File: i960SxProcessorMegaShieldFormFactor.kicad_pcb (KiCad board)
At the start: 4 copper layers, 101.6 x 53.3 mm, 31 parts, among them P1 Power, P2 Data Lines Lower, P3 Data Lines Upper, P4 Address Lines, P5 PWM, P6 Serializable Pins, P7 1284p Direct Connection, U1 74HC245, U2 74HC245, U3 80960Sx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

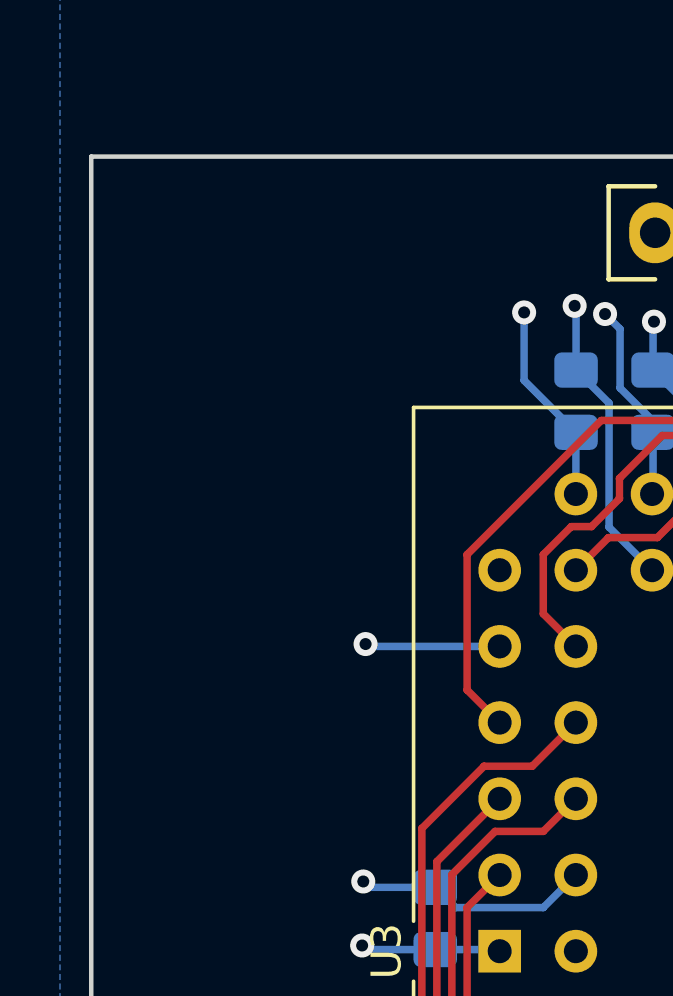
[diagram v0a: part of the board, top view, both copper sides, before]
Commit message: Added CC-BY-SA silk screen
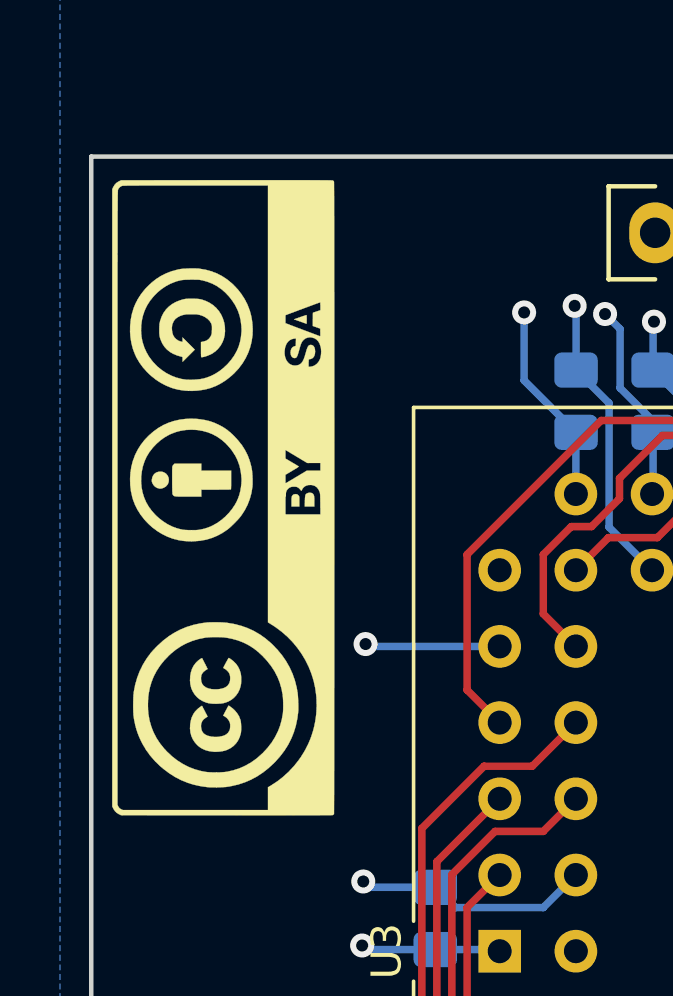
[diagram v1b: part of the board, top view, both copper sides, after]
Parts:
- added G***: LOGO, labitat/labitat_kicad_footprints.pretty:cc-by-sa_badge_8mm, F.Cu at (107.8, 79.7)

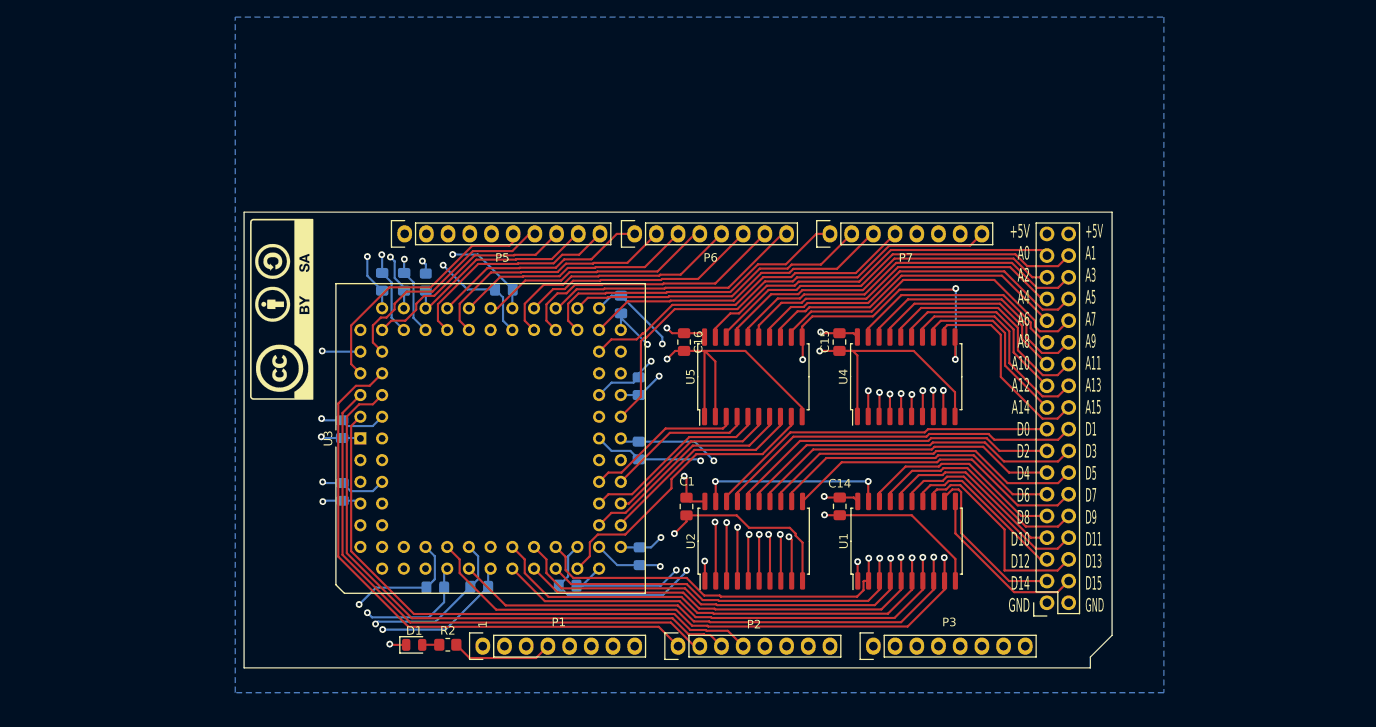
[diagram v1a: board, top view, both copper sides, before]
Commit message: Start placing different ics
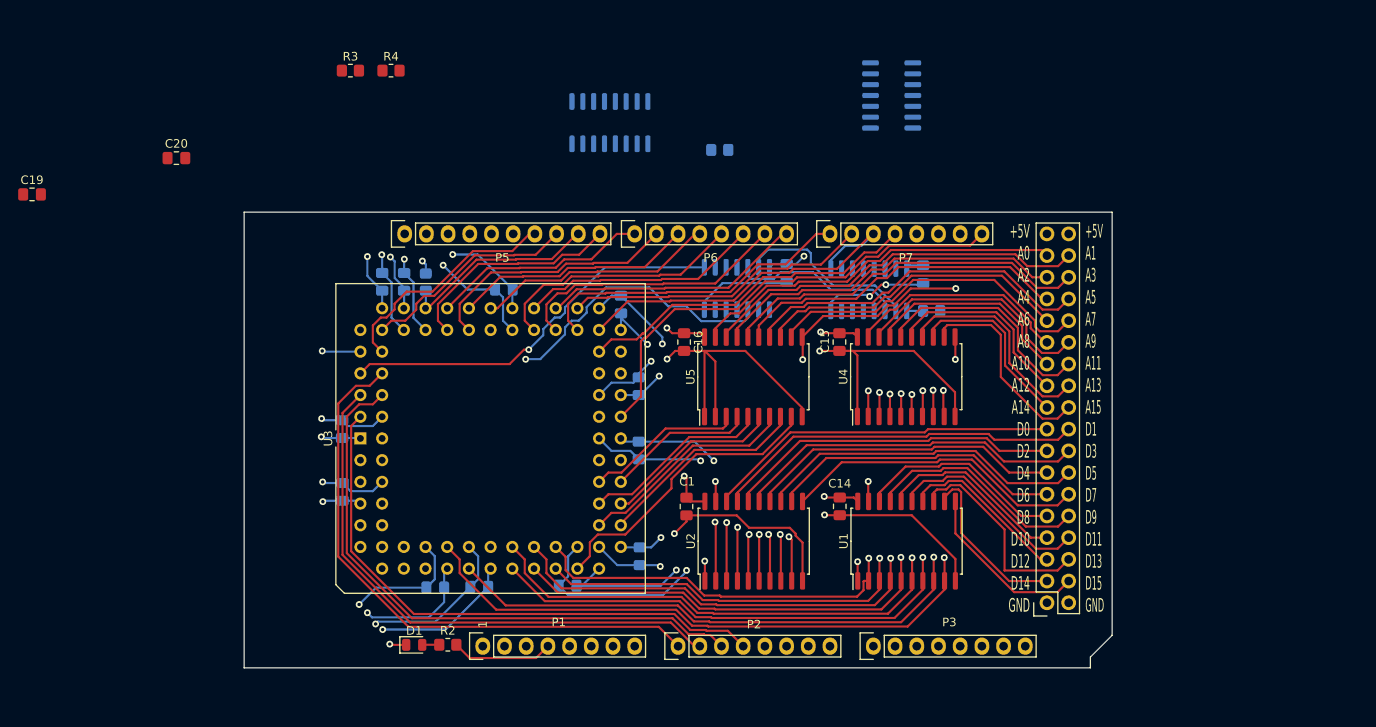
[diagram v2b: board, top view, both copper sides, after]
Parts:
- removed G***: LOGO, labitat/labitat_kicad_footprints.pretty:cc-by-sa_badge_8mm
- added C17: 0.1uF, Capacitor_SMD:C_0805_2012Metric_Pad1.18x1.45mm_HandSolder, B.Cu at (166.9, 75.4)
- added C18: 0.1uF, Capacitor_SMD:C_0805_2012Metric_Pad1.18x1.45mm_HandSolder, B.Cu at (182.9, 75.6)
- added C19: 0.1uF, Capacitor_SMD:C_0805_2012Metric_Pad1.18x1.45mm_HandSolder, F.Cu at (78.6, 66.2)
- added C20: 0.1uF, Capacitor_SMD:C_0805_2012Metric_Pad1.18x1.45mm_HandSolder, F.Cu at (95.5, 62.0)
- added R3: 10k, Resistor_SMD:R_0805_2012Metric_Pad1.20x1.40mm_HandSolder, F.Cu at (115.8, 51.8)
- added R4: 10k, Resistor_SMD:R_0805_2012Metric_Pad1.20x1.40mm_HandSolder, F.Cu at (120.6, 51.8)
- added R5: 10k, Resistor_SMD:R_0805_2012Metric_Pad1.20x1.40mm_HandSolder, B.Cu at (159.1, 61.0)
- added R6: 10k, Resistor_SMD:R_0805_2012Metric_Pad1.20x1.40mm_HandSolder, B.Cu at (183.9, 79.9)
- added U6: 74AHC04, Package_SO:SOIC-14_3.9x8.7mm_P1.27mm, B.Cu at (161.1, 77.3)
- added U7: 74AHC174, Package_SO:SOIC-16_3.9x9.9mm_P1.27mm, B.Cu at (176.5, 77.4)
- added U8: 74AHC08, Package_SO:SOIC-14_3.9x8.7mm_P1.27mm, B.Cu at (179.2, 54.7)
- added U9: 74AHC174, Package_SO:SOIC-16_3.9x9.9mm_P1.27mm, B.Cu at (146.2, 57.8)
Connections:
- P5 pad 3: Net-(P5-Pad3) -> /MCU_FAIL
- U3 pad 79: /~READY -> /~READY960
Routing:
- net /~READY960: track 0.00 -> 46.2 mm, vias 0 -> 1
- net /~BLAST~\~FAIL~: track 25.8 -> 69.6 mm, vias 0 -> 1
- net /~READY: track 30.0 -> 0.00 mm
- net GND: track 239.0 -> 263.4 mm, vias 18 -> 20
- net /Sheet62305775/CLKSRC0: track 0.00 -> 21.5 mm
- net Net-(U6-Pad12): track 0.00 -> 20.0 mm
- net /CLKO: track 36.8 -> 44.0 mm
- net +5V: track 148.1 -> 154.8 mm, vias 17 -> 18
- net /Sheet62305775/~MR1: track 0.00 -> 1.92 mm
- net /ALE: track 99.5 -> 98.7 mm
- removed copper zone on In2.Cu, net +5V
- removed copper zone on B.Cu, net GND

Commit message: Rearrange some connections and try to shove the aux hardware closer together
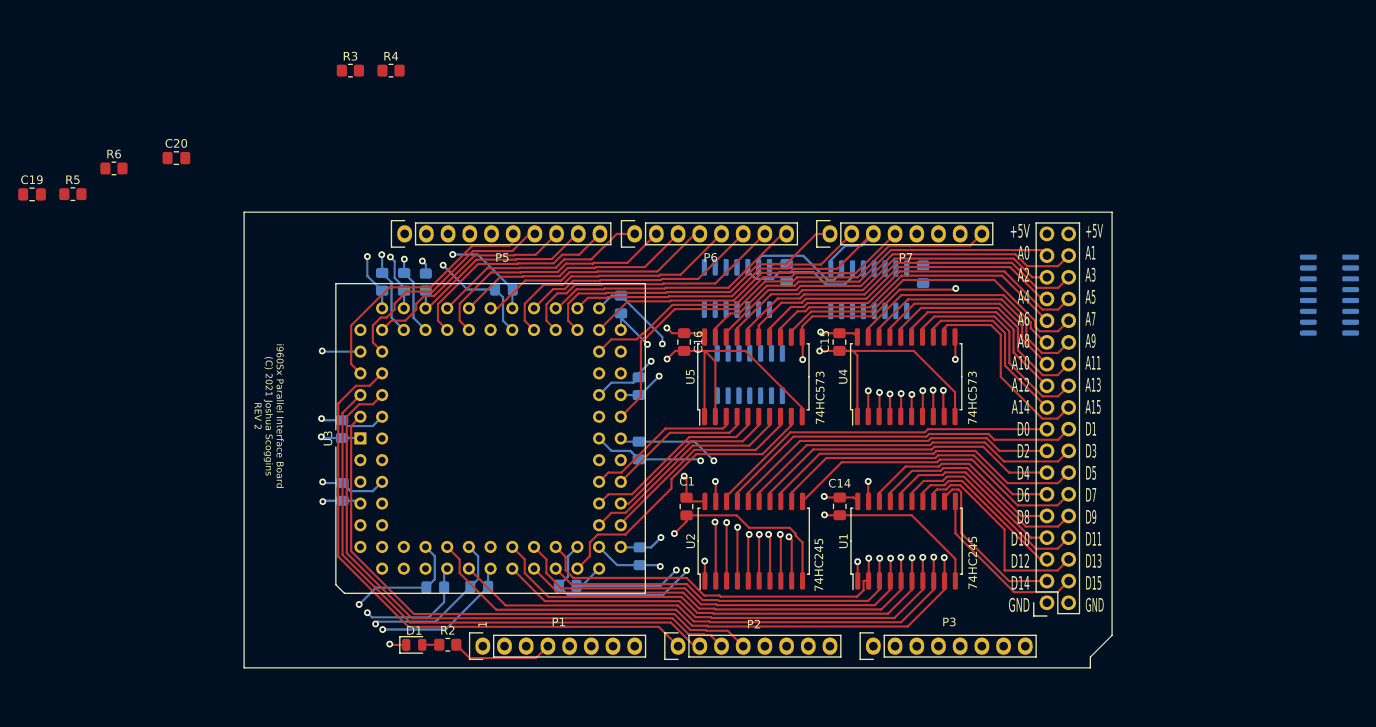
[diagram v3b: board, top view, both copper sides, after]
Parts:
- R5, R6: moved to F.Cu
- moved R6 97.2 mm to (88.1, 63.2), turned to 0 degrees
- moved U9 86.6 mm to (230.4, 78.0), turned to 180 degrees
- moved R5 75.9 mm to (83.3, 66.2)
- moved U8 36.6 mm to (162.6, 87.3), turned to 270 degrees
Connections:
- U7 pad 10: Net-(U7-Pad10) -> /Sheet62305775/CLKSRC0
- U7 pad 11: Net-(U7-Pad11) -> Net-(U6-Pad12)
- U7 pad 2: /Sheet62305775/CLKSRC0 -> Net-(U7-Pad2)
- U7 pad 3: Net-(U6-Pad12) -> Net-(U7-Pad3)
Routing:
- net /~READY960: track 46.2 -> 0.00 mm, vias 1 -> 0
- net /~BLAST~\~FAIL~: track 69.6 -> 25.8 mm, vias 1 -> 0
- net /~READY: track 0.00 -> 30.0 mm
- net GND: track 263.4 -> 239.0 mm, vias 20 -> 18
- net /Sheet62305775/CLKSRC0: track 21.5 -> 12.8 mm
- net Net-(U6-Pad12): track 20.0 -> 15.3 mm
- net +5V: track 154.8 -> 150.3 mm, vias 18 -> 17
- net /Sheet62305775/~MR1: track 1.92 -> 0.00 mm
- net /ALE: track 98.7 -> 99.5 mm

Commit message: Move the transceivers and registers to make room for the aux hardware
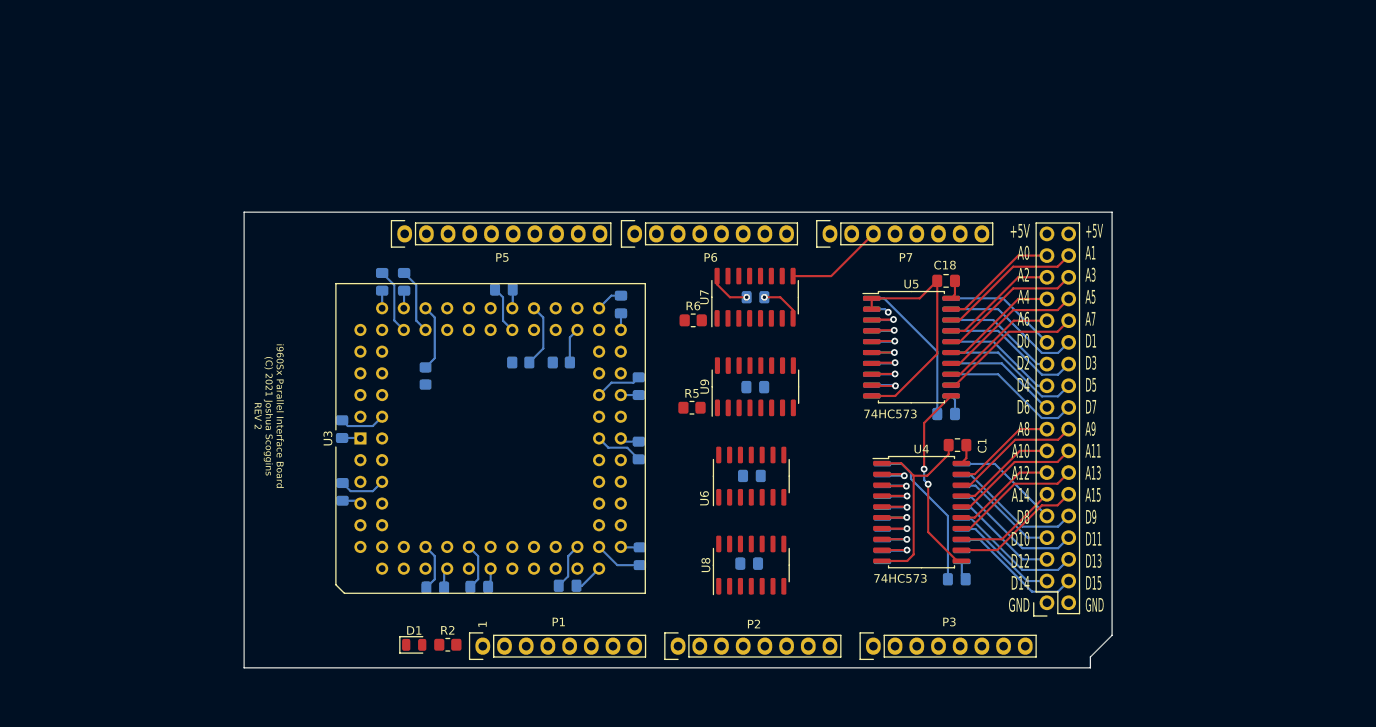
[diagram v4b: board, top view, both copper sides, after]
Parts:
- C14, C15, C16, C19, C20, R3, R4, U1, U2: moved to B.Cu
- C18, U6, U7, U8, U9: moved to F.Cu
- moved C19 94.4 mm to (162.5, 109.5)
- moved C20 77.0 mm to (162.8, 99.2)
- moved R5 76.7 mm to (155.8, 91.2)
- moved R6 70.1 mm to (155.9, 81.0)
- moved U9 68.1 mm to (163.2, 88.8), turned to 90 degrees
- moved R3 39.6 mm to (135.8, 85.9)
- moved R4 39.6 mm to (140.5, 85.9)
- moved C1 32.5 mm to (186.9, 95.6), turned to 180 degrees
- moved C16 31.8 mm to (185.6, 92.0), turned to 180 degrees
- moved U2 29.3 mm to (181.5, 84.1), turned to 0 degrees
- moved U8 22.3 mm to (162.7, 109.6), turned to 90 degrees
- moved U6 22.0 mm to (162.7, 99.2)
- moved U5 18.8 mm to (181.5, 84.1), turned to 0 degrees
- moved C14 16.1 mm to (186.8, 111.3), turned to 180 degrees
- moved U4 16.0 mm to (182.7, 103.4), turned to 0 degrees
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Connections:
- P4 pad 11: /D6 -> /A14
- P4 pad 12: /D7 -> /A15
- P4 pad 13: /D4 -> /A12
- P4 pad 14: /D5 -> /A13
- P4 pad 15: /D2 -> /A10
- P4 pad 16: /D3 -> /A11
- P4 pad 17: /D0_OUT -> /A8
- P4 pad 18: /D1 -> /A9
- P4 pad 19: /A14 -> /D6
- P4 pad 20: /A15 -> /D7
- P4 pad 21: /A12 -> /D4
- P4 pad 22: /A13 -> /D5
- P4 pad 23: /A10 -> /D2
- P4 pad 24: /A11 -> /D3
- P4 pad 25: /A8 -> /D0_OUT
- P4 pad 26: /A9 -> /D1
- U1 pad 11: /D15 -> /D8
- U1 pad 12: /D14 -> /D9
- U1 pad 13: /D13 -> /D10
- U1 pad 14: /D12 -> /D11
- U1 pad 15: /D11 -> /D12
- U1 pad 16: /D10 -> /D13
- U1 pad 17: /D9 -> /D14
- U1 pad 18: /D8 -> /D15
- U1 pad 2: /AD8 -> /AD15
- U1 pad 3: /AD9 -> /AD14
- U1 pad 4: /AD10 -> /AD13
- U1 pad 5: /AD11 -> /AD12
- U1 pad 6: /AD12 -> /AD11
- U1 pad 7: /AD13 -> /AD10
- U1 pad 8: /AD14 -> /AD9
- U1 pad 9: /AD15 -> /AD8
- U2 pad 11: /D7 -> /D0_OUT
- U2 pad 12: /D6 -> /D1
- U2 pad 13: /D5 -> /D2
- U2 pad 14: /D4 -> /D3
- U2 pad 15: /D3 -> /D4
- U2 pad 16: /D2 -> /D5
- U2 pad 17: /D1 -> /D6
- U2 pad 18: /D0_OUT -> /D7
- U2 pad 2: /D0 -> /AD7
- U2 pad 3: /AD1 -> /AD6
- U2 pad 4: /AD2 -> /AD5
- U2 pad 5: /AD3 -> /AD4
- U2 pad 6: /AD4 -> /AD3
- U2 pad 7: /AD5 -> /AD2
- U2 pad 8: /AD6 -> /AD1
- U2 pad 9: /AD7 -> /D0
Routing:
- net /DT\~R: track 108.4 -> 0.00 mm, vias 2 -> 0
- net GND: track 239.0 -> 134.5 mm, vias 18 -> 1
- net /~DEN: track 88.7 -> 0.00 mm, vias 2 -> 0
- net +5V: track 150.3 -> 68.1 mm, vias 17 -> 1
- net /ALE: track 99.5 -> 22.7 mm, vias 3 -> 2
- net /BA3: track 54.9 -> 0.00 mm
- net /BA2: track 52.2 -> 0.00 mm
- net /BA1: track 48.4 -> 0.00 mm
- net /~BE1: track 47.6 -> 0.00 mm
- net /~BE0: track 40.4 -> 0.00 mm
- net /~RESET960: track 35.7 -> 0.00 mm
- net /~INT0: track 37.6 -> 4.17 mm
- net /CLKO: track 44.0 -> 11.4 mm
- net /INT2: track 32.4 -> 0.00 mm
- net /INT1: track 30.6 -> 0.00 mm
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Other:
- board text added: "+5V A0 A2 A4 A6 D0 D2 D4 D6 A8 A10 A12 A14 D8 D10 D12 D14 GND"
- board text added: "+5V A1 A3 A5 A7 D1 D3 D5 D7 A9 A11 A13 A15 D9 D11 D13 D15 GND"
- board text removed: "+5V A0 A2 A4 A6 A8 A10 A12 A14 D0 D2 D4 D6 D8 D10 D12 D14 GND"
- board text removed: "+5V A1 A3 A5 A7 A9 A11 A13 A15 D1 D3 D5 D7 D9 D11 D13 D15 GND"

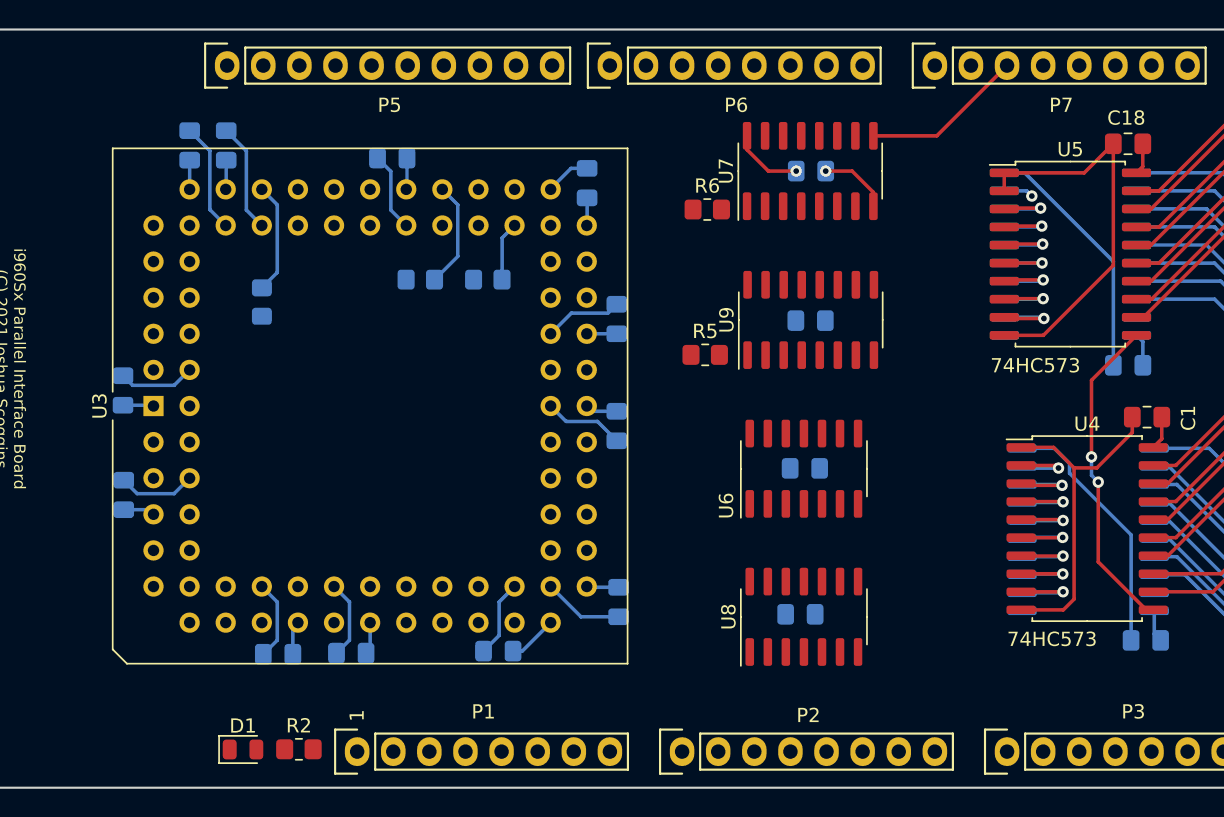
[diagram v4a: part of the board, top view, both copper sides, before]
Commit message: Mostly complete rewiring
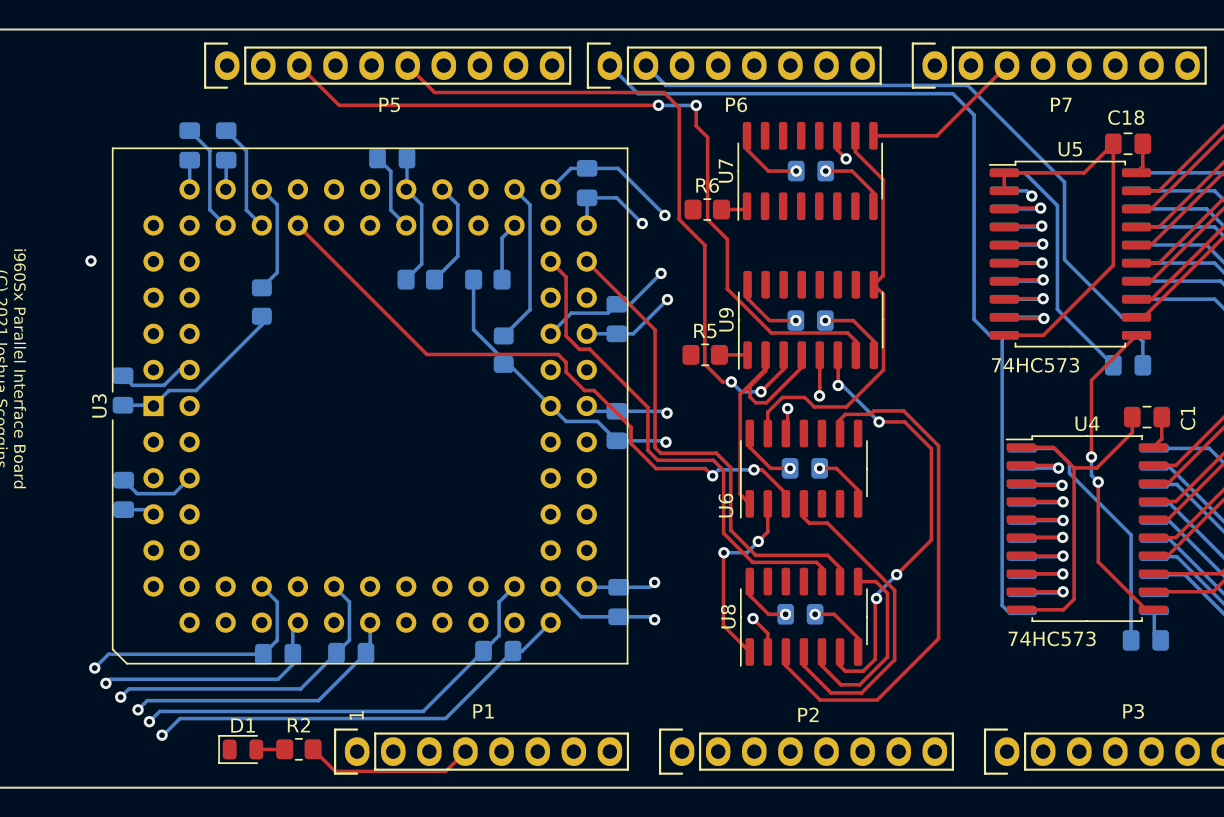
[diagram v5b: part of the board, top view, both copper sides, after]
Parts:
- added R7: 10k, Resistor_SMD:R_0805_2012Metric_Pad1.20x1.40mm_HandSolder, B.Cu at (141.6, 90.9)
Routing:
- net +5V: track 68.1 -> 180.4 mm, vias 1 -> 11
- net GND: track 134.5 -> 229.2 mm, vias 1 -> 12
- net /DT\~R: track 0.00 -> 90.2 mm
- net /~BE1: track 0.00 -> 77.4 mm
- net /~BE0: track 0.00 -> 77.1 mm
- net /~DEN: track 0.00 -> 75.0 mm
- net /~BLAST~\~FAIL~: track 0.00 -> 70.1 mm, vias 0 -> 2
- net /BA3: track 0.00 -> 56.1 mm
- net /BA2: track 0.00 -> 55.2 mm
- net /MCU_FAIL: track 0.00 -> 54.4 mm, vias 0 -> 2
- net /~RESET960: track 0.00 -> 47.2 mm
- net /~READY: track 0.00 -> 47.1 mm, vias 0 -> 2
- net /BA1: track 0.00 -> 46.8 mm
- net /~INT0: track 4.17 -> 41.7 mm
- net Net-(U6-Pad9): track 0.00 -> 37.2 mm
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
